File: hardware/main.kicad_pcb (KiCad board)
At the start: 2 copper layers, 84.6 x 84.6 mm, 130 parts, among them J1 USB_DEBUG, J2 USB_TO_ANDROID, M1 Mounting Hole, M2 Mounting Hole, M3 Mounting Hole, M4 Mounting Hole, P1 VBAT-TEST, P11 MOTOR-R, P12 MOTOR-L, P13 AND5V, P14 P24, P2 USB-VBUS, P3 SERVO-TILT, P4 JTAG10, P5 POWER-CHARGE, P6 POWER, P7 BATCHG, P8 12VIN, P9 BAT, Q1 ZXMP2120FFTA, Q2 BD242CG, Q3 IRLML2803TRPBF, Q4 IRLML2803TRPBF, U1 STM32F102C6, U2 BQ24450, U3 ZLDO1117, U4 AP6502, U5 7408, U6 MC33926, U7 MC33926, U8 FT312D, X1 8MHz, X2 12MHz

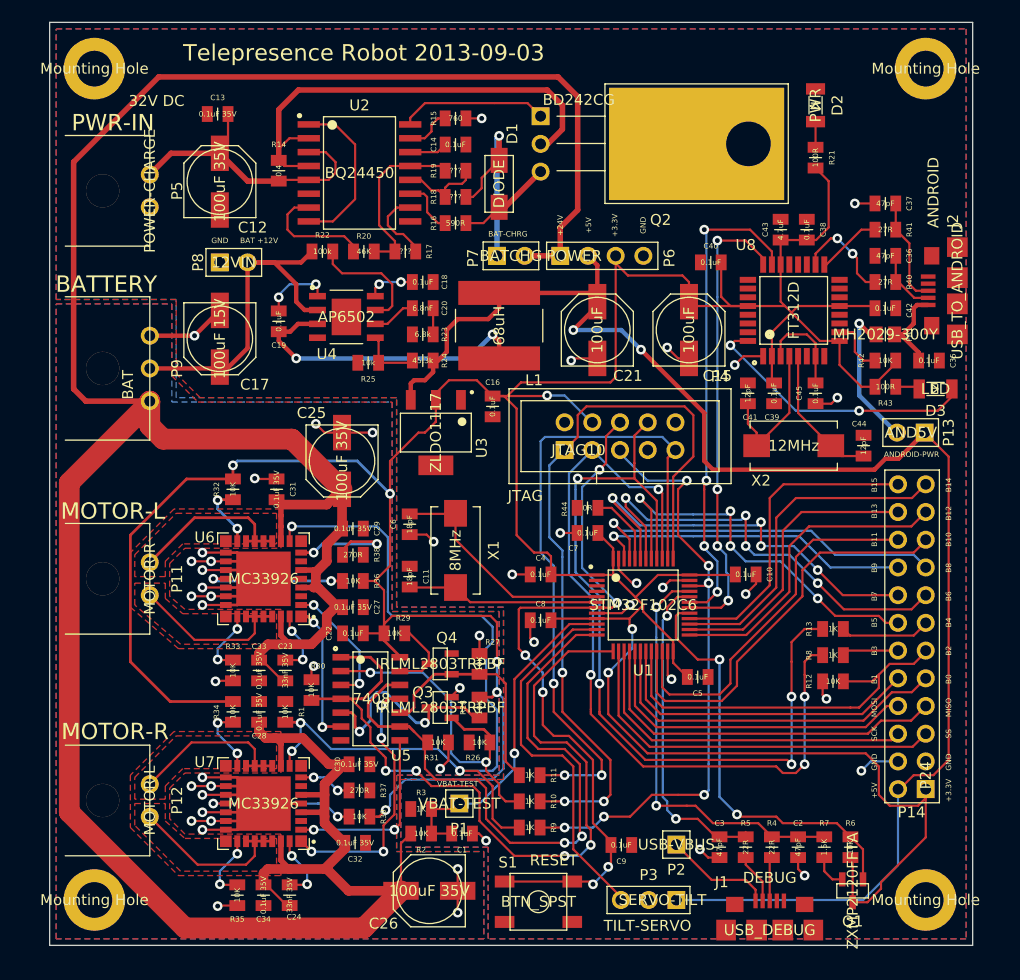
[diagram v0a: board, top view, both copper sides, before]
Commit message: calculations for battery charger
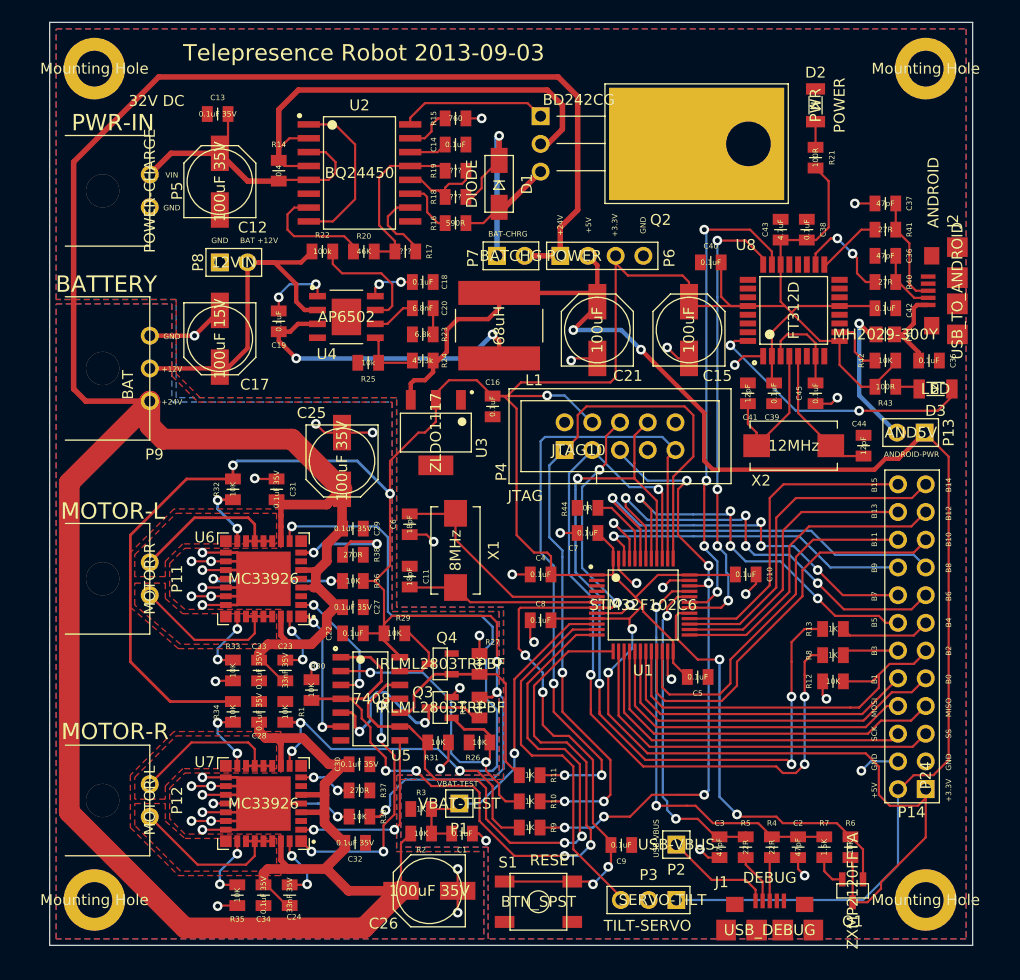
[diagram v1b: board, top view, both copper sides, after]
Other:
- board text added: "+12V"
- board text added: "POWER"
- board text added: "USB-VBUS"
- board text added: "VIN"
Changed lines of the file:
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@@
     (area 106.748778 36.349999 198.051222 196.282)
     (thickness 1.6)
-    (drawings 49)
+    (drawings 56)
     (tracks 1381)
     (zones 0)
@@
     )
   )
-  (module DIOM5226X220N (layer F.Cu)
-    (at 151.4 51.2 90)
-    (fp_text reference D1 (at 4.6 1.2 270) (layer F.SilkS)
-      (effects (font (size 1 1) (thickness 0.15)))
-    )
-    (fp_text value DIODE (at 0 0 90) (layer F.SilkS)
-      (effects (font (size 1 1) (thickness 0.15)))
-    )
-    (fp_line (start -3.55 -1.75) (end 3.55 -1.75) (layer Cmts.User) (width 0.1))
-    (fp_line (start 3.55 -1.75) (end 3.55 1.75) (layer Cmts.User) (width 0.1))
-    (fp_line (start 3.55 1.75) (end -3.55 1.75) (layer Cmts.User) (width 0.1))
-    (fp_line (start -3.55 1.75) (end -3.55 -1.75) (layer Cmts.User) (width 0.1))
-    (fp_line (start -2.6 -1.3) (end 2.6 -1.3) (layer F.SilkS) (width 0.1))
-    (fp_line (start 2.6 -1.3) (end 2.6 1.3) (layer F.SilkS) (width 0.1))
-    (fp_line (start 2.6 1.3) (end -2.6 1.3) (layer F.SilkS) (width 0.1))
-    (fp_line (start -2.6 1.3) (end -2.6 -1.3) (layer F.SilkS) (width 0.1))
-    (pad 1 smd rect (at -2.15 0 90) (size 2.3 1.55)
-      (layers F.Cu F.Paste F.Mask)
-      (net 106 N-0000073)
-    )
-    (pad 2 smd rect (at 2.15 0 90) (size 2.3 1.55)
-      (layers F.Cu F.Paste F.Mask)
-      (net 104 N-0000071)
-    )
-  )
   (module LEDC3216X100N (layer F.Cu)
     (at 180.4 44 90)
-    (fp_text reference D2 (at 0 2 90) (layer F.SilkS)
+    (fp_text reference D2 (at 3 0 180) (layer F.SilkS)
       (effects (font (size 1 1) (thickness 0.15)))
     )
@@
   (module TECONN-2-1445098-3 (layer F.Cu)
     (at 119.38 71.12 90)
-    (fp_text reference P9 (at 3 2.5 90) (layer F.SilkS)
+    (fp_text reference P9 (at -4.88 0.42 180) (layer F.SilkS)
       (effects (font (size 1 1) (thickness 0.15)))
     )
@@
   (module SHDRV10W66P254_2X5_2035X870X609P (layer F.Cu)
     (at 157.4 75.6)
-    (fp_text reference P4 (at 14.24 -6.74) (layer F.SilkS)
+    (fp_text reference P4 (at -5.8 2 90) (layer F.SilkS)
       (effects (font (size 1 1) (thickness 0.15)))
     )
@@
     )
   )
+  (module DIOM5226X220N (layer F.Cu)
+    (at 151.4 51.2 90)
+    (fp_text reference D1 (at 0 2.54 90) (layer F.SilkS)
+      (effects (font (size 1 1) (thickness 0.15)))
+    )
+    (fp_text value DIODE (at 0 -2.5 90) (layer F.SilkS)
+      (effects (font (size 1 1) (thickness 0.15)))
+    )
+    (fp_line (start 0.25 -0.5) (end 0.25 0.5) (layer F.SilkS) (width 0.1))
+    (fp_line (start -0.5 -0.5) (end -0.5 0.5) (layer F.SilkS) (width 0.1))
+    (fp_line (start -0.5 0.5) (end 0.25 0) (layer F.SilkS) (width 0.1))
+    (fp_line (start 0.25 0) (end -0.5 -0.5) (layer F.SilkS) (width 0.1))
+    (fp_line (start -3.55 -1.75) (end 3.55 -1.75) (layer Cmts.User) (width 0.1))
+    (fp_line (start 3.55 -1.75) (end 3.55 1.75) (layer Cmts.User) (width 0.1))
+    (fp_line (start 3.55 1.75) (end -3.55 1.75) (layer Cmts.User) (width 0.1))
+    (fp_line (start -3.55 1.75) (end -3.55 -1.75) (layer Cmts.User) (width 0.1))
+    (fp_line (start -2.6 -1.3) (end 2.6 -1.3) (layer F.SilkS) (width 0.1))
+    (fp_line (start 2.6 -1.3) (end 2.6 1.3) (layer F.SilkS) (width 0.1))
+    (fp_line (start 2.6 1.3) (end -2.6 1.3) (layer F.SilkS) (width 0.1))
+    (fp_line (start -2.6 1.3) (end -2.6 -1.3) (layer F.SilkS) (width 0.1))
+    (pad 1 smd rect (at -2.15 0 90) (size 2.3 1.55)
+      (layers F.Cu F.Paste F.Mask)
+      (net 106 N-0000073)
+    )
+    (pad 2 smd rect (at 2.15 0 90) (size 2.3 1.55)
+      (layers F.Cu F.Paste F.Mask)
+      (net 104 N-0000071)
+    )
+  )
+  (gr_text USB-VBUS (at 165.8 111.2 90) (layer F.SilkS)
+    (effects (font (size 0.5 0.5) (thickness 0.12)))
+  )
+  (gr_text VIN (at 121.4 50.4) (layer F.SilkS)
+    (effects (font (size 0.5 0.5) (thickness 0.12)))
+  )
+  (gr_text GND (at 121.4 53.4) (layer F.SilkS)
+    (effects (font (size 0.5 0.5) (thickness 0.12)))
+  )
+  (gr_text +24V (at 121.4 71.2) (layer F.SilkS)
+    (effects (font (size 0.5 0.5) (thickness 0.12)))
+  )
+  (gr_text +12V (at 121.4 68.2) (layer F.SilkS)
+    (effects (font (size 0.5 0.5) (thickness 0.12)))
+  )
+  (gr_text GND (at 121.4 65.2) (layer F.SilkS)
+    (effects (font (size 0.5 0.5) (thickness 0.12)))
+  )
+  (gr_text POWER (at 182.6 44 90) (layer F.SilkS)
+    (effects (font (size 1 1) (thickness 0.2)))
+  )
   (gr_text VBAT-TEST (at 147.6 106.2) (layer F.SilkS)

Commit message: changed silk size
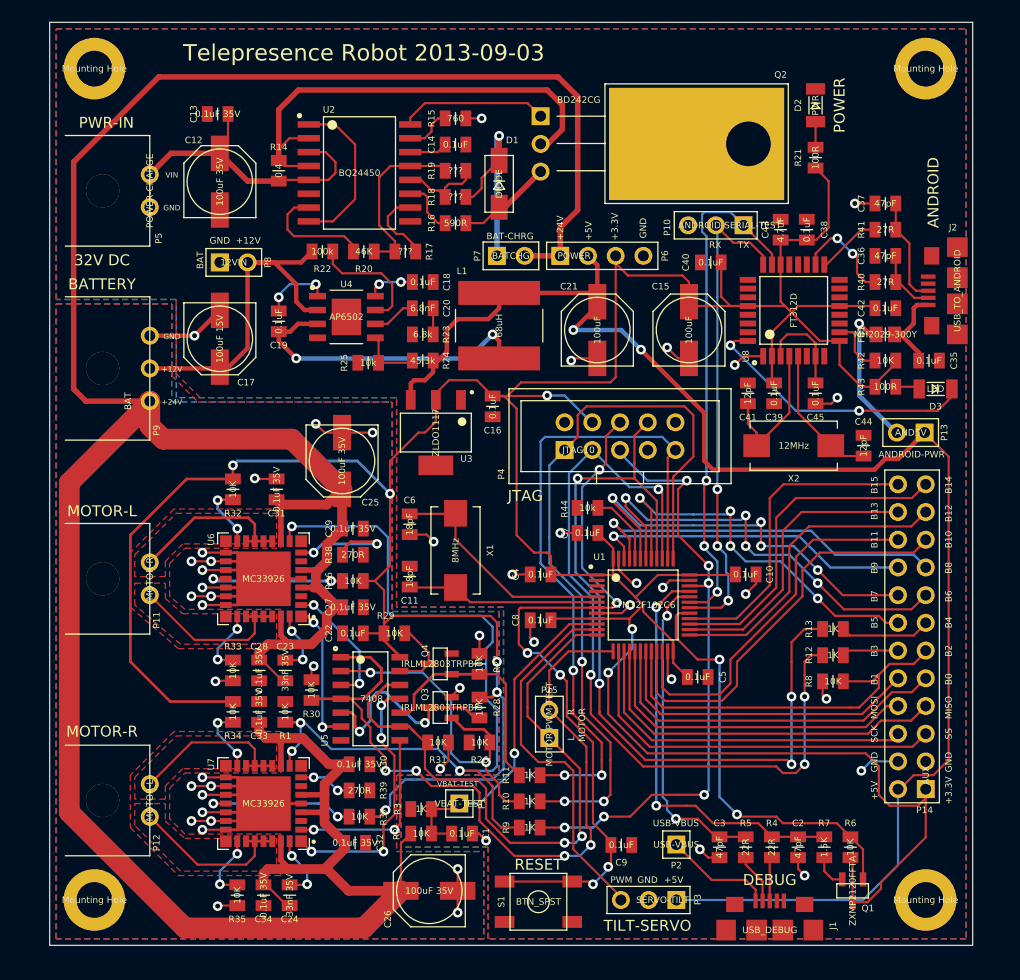
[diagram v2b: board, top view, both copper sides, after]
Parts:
- added P10: ANDROID-SERIAL-TEST, HDRV3W66P254_1X3_762X249X838P, F.Cu at (173.8, 55.0)
- added P15: MOTOR-PWM-TEST, HDRV2W66P254_1X2_508X249X838P, F.Cu at (156.0, 102.0)
- P14: value P24 -> AUX
- R44: value 0R -> 10k
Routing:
- net /Motor Controllers/MOTOR-R-PWM: track 72.0 -> 69.4 mm
- net /Android/TX: track 45.0 -> 47.3 mm, vias 4 -> 3
- net /Android/RX: track 42.7 -> 45.0 mm, vias 4 -> 3
- net /Motor Controllers/MOTOR-L-PWM: track 58.5 -> 57.1 mm
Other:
- board text added: "BAT"
- board text added: "L"
- board text added: "MOTOR"
- board text added: "PWM"
- board text added: "R"
- board text added: "RX"
- board text added: "TX"
- board text removed: "BAT +12V"

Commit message: increase power track thickness
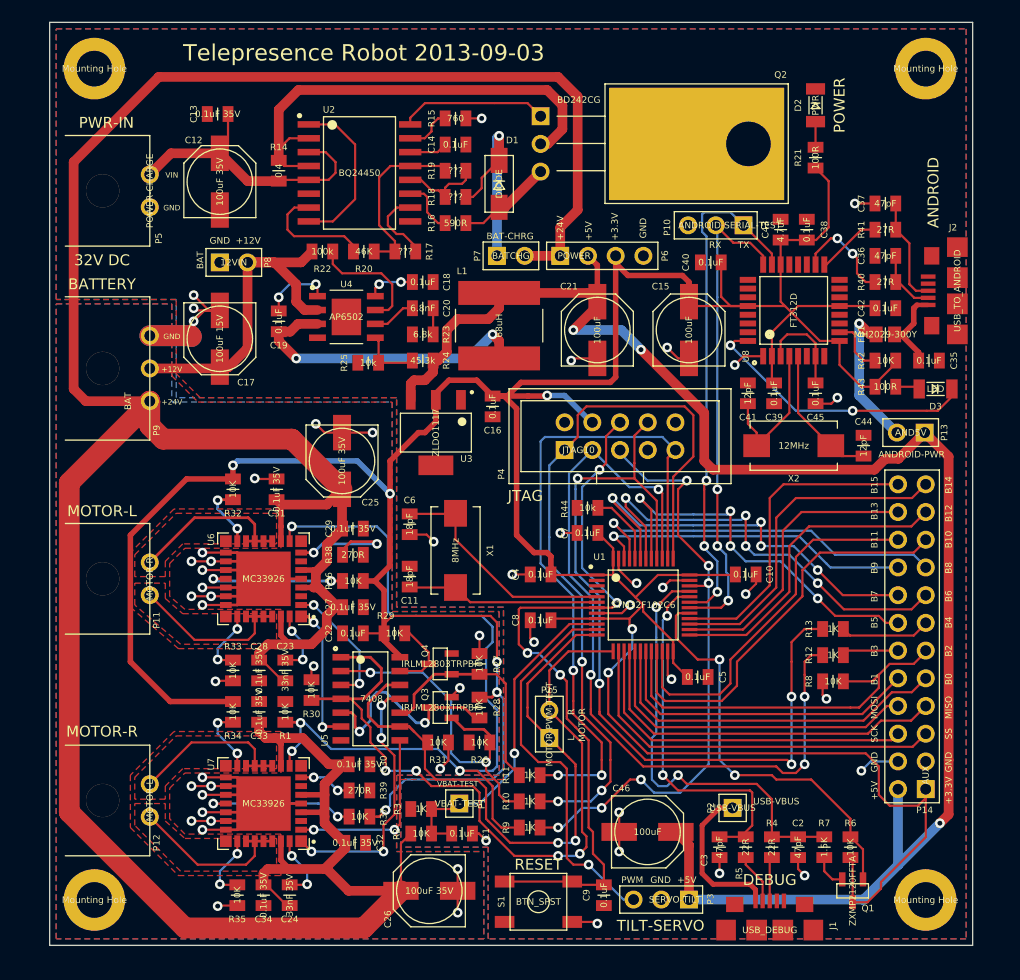
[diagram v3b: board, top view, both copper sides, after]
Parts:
- added C46: 100uF, CAPAE660X790N, F.Cu at (165.0, 110.6)
- moved P2 6.16 mm to (172.8, 108.4)
- moved C9 4.87 mm to (161.0, 116.4), turned to 270 degrees
- moved P3 1.16 mm to (168.8, 116.8)
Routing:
- net GND: track 161.6 -> 175.5 mm, vias 48 -> 53
- net +5V: track 139.8 -> 151.3 mm, vias 2 -> 3
- net N-0000018: track 10.00 -> 14.4 mm
- net N-0000046: track 29.6 -> 33.6 mm
- net N-0000056: track 38.4 -> 40.4 mm
- net /SERVO-TILT-PWM: track 34.2 -> 35.7 mm, vias 0 -> 1
- net /USB-DISCONNECT: track 38.7 -> 37.6 mm
- net /JTCK: track 70.1 -> 69.4 mm
- net /Motor Controllers/MOTOR-L-PWM: track 57.1 -> 56.5 mm
- net /nRST: track 66.7 -> 67.1 mm, vias 6 -> 4

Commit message: working
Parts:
- P11: value MOTOR-R -> MOTOR-L
- P12: value MOTOR-L -> MOTOR-R
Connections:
- P15 pad 1: /Motor Controllers/MOTOR-L-PWM -> /Motor Controllers/MOTOR-R-PWM
- P15 pad 2: /Motor Controllers/MOTOR-R-PWM -> /Motor Controllers/MOTOR-L-PWM
- Q3 pad 1: /Motor Controllers/MOTOR-R-DIR -> /Motor Controllers/MOTOR-L-DIR
- Q4 pad 1: /Motor Controllers/MOTOR-L-DIR -> /Motor Controllers/MOTOR-R-DIR
- R10 pad 2: /Motor Controllers/MOTOR-R-DIR -> /Motor Controllers/MOTOR-L-DIR
- R11 pad 2: /Motor Controllers/MOTOR-L-DIR -> /Motor Controllers/MOTOR-R-DIR
- R26 pad 1: /Motor Controllers/MOTOR-R-DIR -> /Motor Controllers/MOTOR-L-DIR
- R27 pad 1: /Motor Controllers/MOTOR-L-DIR -> /Motor Controllers/MOTOR-R-DIR
- R30 pad 1: /Motor Controllers/MOTOR-R-PWM -> /Motor Controllers/MOTOR-L-PWM
- R31 pad 1: /Motor Controllers/MOTOR-L-PWM -> /Motor Controllers/MOTOR-R-PWM
- U1 pad 12: /Motor Controllers/MOTOR-L-PWM -> /Motor Controllers/MOTOR-R-PWM
- U1 pad 13: /Motor Controllers/MOTOR-R-PWM -> /Motor Controllers/MOTOR-L-PWM
- U5 pad 1: /Motor Controllers/MOTOR-R-PWM -> /Motor Controllers/MOTOR-L-PWM
- U5 pad 10: /Motor Controllers/MOTOR-L-DIR -> /Motor Controllers/MOTOR-R-DIR
- U5 pad 12: /Motor Controllers/MOTOR-L-PWM -> /Motor Controllers/MOTOR-R-PWM
- U5 pad 2: /Motor Controllers/MOTOR-R-DIR -> /Motor Controllers/MOTOR-L-DIR
- U5 pad 4: /Motor Controllers/MOTOR-R-PWM -> /Motor Controllers/MOTOR-L-PWM
- U5 pad 9: /Motor Controllers/MOTOR-L-PWM -> /Motor Controllers/MOTOR-R-PWM
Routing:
- net /Motor Controllers/MOTOR-R-PWM: track 69.0 -> 56.5 mm, vias 4 -> 2
- net /Motor Controllers/MOTOR-L-PWM: track 56.5 -> 69.0 mm, vias 2 -> 4
- net /Motor Controllers/MOTOR-R-DIR: track 31.9 -> 21.1 mm, vias 2 -> 0
- net /Motor Controllers/MOTOR-L-DIR: track 21.1 -> 31.9 mm, vias 0 -> 2
